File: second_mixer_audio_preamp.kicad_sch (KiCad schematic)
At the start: 34 parts, among them Q1301 MMBT3904, Q1302 MMBT3904, Q1303 MMBT3904, U1301 ADE-1

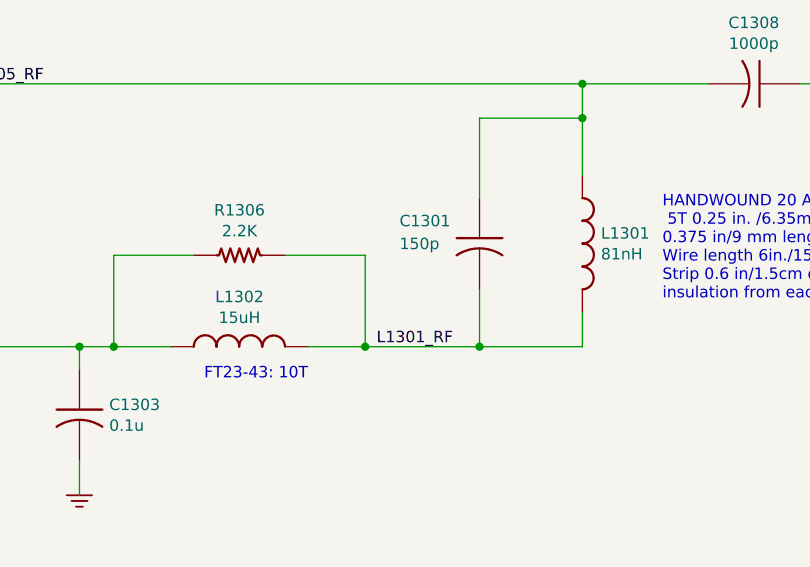
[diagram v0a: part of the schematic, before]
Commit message: Update pcb database to version 6
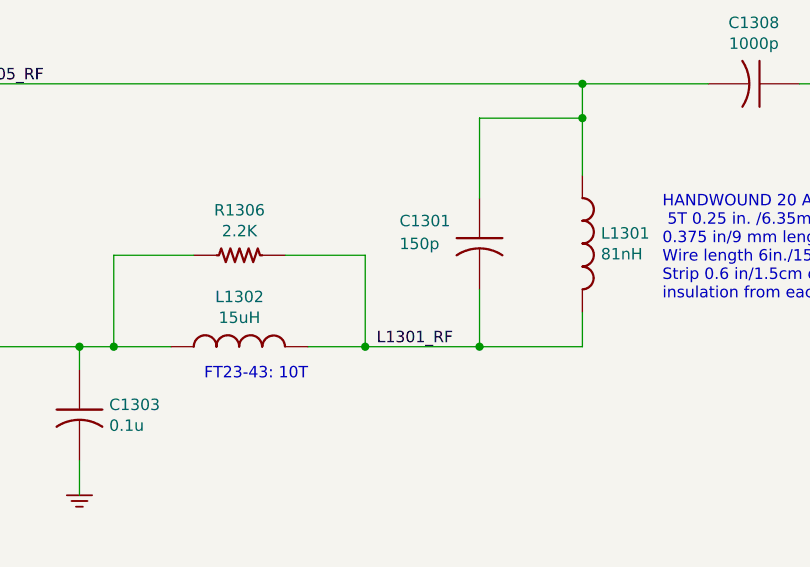
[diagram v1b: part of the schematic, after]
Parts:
- C1301: symbol Custom:C_US_0805_0.1UF_X7R_10%_50V_HS -> custom:C_US_0805_0.1UF_X7R_10%_50V_HS; PartNumber 800239-151 -> 800238-104
- C1302, C1304, C1305, C1306, C1307: symbol Custom:CP_US -> custom:CP_US; PartNumber 800267-226 -> 80000X-XXX
- C1303: symbol Custom:C_US_0805_0.1UF_X7R_10%_50V_HS -> custom:C_US_0805_0.1UF_X7R_10%_50V_HS
- C1308: symbol Custom:C_US -> custom:C_US; PartNumber 800239-102 -> 800063-XXX
- L1301: symbol Custom:L_US -> custom:L_US; PartNumber 800YYY-YYY -> 8000XX-XXX
- L1302: symbol Custom:L_US -> custom:L_US; PartNumber 800257-023 -> 8000XX-XXX
- Q1301, Q1302, Q1303: symbol Custom:MMBT3904 -> custom:MMBT3904
- R1301, R1304: symbol Custom:R_US_0805_1%_HS -> custom:R_US_0805_1%_HS; PartNumber 800235-180 -> 800235-XXX
- R1302, R1303, R1307, R1308: symbol Custom:R_US_0805_1%_HS -> custom:R_US_0805_1%_HS; PartNumber 800235-301 -> 800235-XXX
- R1305: symbol Custom:R_US_0805_1%_HS -> custom:R_US_0805_1%_HS; PartNumber 800235-360 -> 800235-XXX
- R1306: symbol Custom:R_US_0805_1%_HS -> custom:R_US_0805_1%_HS; PartNumber 800235-222 -> 800235-XXX
- R1309, R1310: symbol Custom:R_US_0805_1%_HS -> custom:R_US_0805_1%_HS; PartNumber 800235-151 -> 800235-XXX
- R1311: symbol Custom:R_US_0805_1%_HS -> custom:R_US_0805_1%_HS; PartNumber 800235-473 -> 800235-XXX
- R1312, R1314: symbol Custom:R_US_0805_1%_HS -> custom:R_US_0805_1%_HS; PartNumber 800235-102 -> 800235-XXX
- R1313, R1317: symbol Custom:R_US_0805_1%_HS -> custom:R_US_0805_1%_HS; PartNumber 800235-332 -> 800235-XXX
- R1315: symbol Custom:R_US_0805_1%_HS -> custom:R_US_0805_1%_HS; PartNumber 800235-103 -> 800235-XXX
- R1316: symbol Custom:R_US_0805_1%_HS -> custom:R_US_0805_1%_HS; PartNumber 800235-682 -> 800235-XXX
- R1318: symbol Custom:R_US_0805_1%_HS -> custom:R_US_0805_1%_HS; PartNumber 800235-101 -> 800235-XXX
- R1319: symbol Custom:R_US_0805_1%_HS -> custom:R_US_0805_1%_HS; PartNumber 800235-472 -> 800235-XXX
- TP1301: symbol Custom:TESTPINTPSQ025 -> custom:TESTPINTPSQ025
- U1301: symbol Custom:ADE-1 -> custom:ADE-1

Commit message: Fix BOM part number errors and out of sync footprints which happened during conversion from Kicad 5 to 6
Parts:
- C1301: PartNumber 800238-104 -> 800239-151
- C1302, C1304, C1305, C1306, C1307: PartNumber 80000X-XXX -> 800267-226
- C1308: PartNumber 800063-XXX -> 800239-103
- R1301, R1304: PartNumber 800235-XXX -> 800235-180
- R1302, R1303, R1307, R1308: PartNumber 800235-XXX -> 800235-301
- R1305: PartNumber 800235-XXX -> 800235-360
- R1306: PartNumber 800235-XXX -> 800235-222
- R1309, R1310: PartNumber 800235-XXX -> 800235-151
- R1311: PartNumber 800235-XXX -> 800235-473
- R1312, R1314: PartNumber 800235-XXX -> 800235-102
- R1313, R1317: PartNumber 800235-XXX -> 800235-332
- R1315: PartNumber 800235-XXX -> 800235-103
- R1316: PartNumber 800235-XXX -> 800235-682
- R1318: PartNumber 800235-XXX -> 800235-101
- R1319: PartNumber 800235-XXX -> 800235-472
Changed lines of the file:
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@@
       (effects (font (size 1.524 1.524)))
     )
-    (property "PartNumber" "800235-XXX" (id 4) (at 42.672 27.94 90)
+    (property "PartNumber" "800235-301" (id 4) (at 42.672 27.94 90)
       (effects (font (size 1.524 1.524)) hide)
     )
@@
       (effects (font (size 1.524 1.524)))
     )
-    (property "PartNumber" "800235-XXX" (id 4) (at 59.182 27.94 90)
+    (property "PartNumber" "800235-301" (id 4) (at 59.182 27.94 90)
       (effects (font (size 1.524 1.524)) hide)
     )
@@
       (effects (font (size 1.524 1.524)))
     )
-    (property "PartNumber" "800235-XXX" (id 4) (at 49.53 26.162 90)
+    (property "PartNumber" "800235-180" (id 4) (at 49.53 26.162 90)
       (effects (font (size 1.524 1.524)) hide)
     )
@@
       (effects (font (size 1.524 1.524)))
     )
-    (property "PartNumber" "800235-XXX" (id 4) (at 42.672 57.15 90)
+    (property "PartNumber" "800235-301" (id 4) (at 42.672 57.15 90)
       (effects (font (size 1.524 1.524)) hide)
     )
@@
       (effects (font (size 1.524 1.524)))
     )
-    (property "PartNumber" "800235-XXX" (id 4) (at 59.182 57.15 90)
+    (property "PartNumber" "800235-301" (id 4) (at 59.182 57.15 90)
       (effects (font (size 1.524 1.524)) hide)
     )
@@
       (effects (font (size 1.524 1.524)))
     )
-    (property "PartNumber" "800235-XXX" (id 4) (at 49.53 55.372 90)
+    (property "PartNumber" "800235-180" (id 4) (at 49.53 55.372 90)
       (effects (font (size 1.524 1.524)) hide)
     )
@@
       (effects (font (size 1.524 1.524)))
     )
-    (property "PartNumber" "800235-XXX" (id 4) (at 111.252 57.15 90)
+    (property "PartNumber" "800235-151" (id 4) (at 111.252 57.15 90)
       (effects (font (size 1.524 1.524)) hide)
     )
@@
       (effects (font (size 1.524 1.524)))
     )
-    (property "PartNumber" "800235-XXX" (id 4) (at 127.762 57.15 90)
+    (property "PartNumber" "800235-151" (id 4) (at 127.762 57.15 90)
       (effects (font (size 1.524 1.524)) hide)
     )
@@
       (effects (font (size 1.524 1.524)))
     )
-    (property "PartNumber" "800235-XXX" (id 4) (at 118.11 55.372 90)
+    (property "PartNumber" "800235-360" (id 4) (at 118.11 55.372 90)
       (effects (font (size 1.524 1.524)) hide)
     )
@@
       (effects (font (size 1.524 1.524)))
     )
-    (property "PartNumber" "80000X-XXX" (id 4) (at 59.69 76.2 0)
+    (property "PartNumber" "800267-226" (id 4) (at 59.69 76.2 0)
       (effects (font (size 1.524 1.524)) hide)
     )
@@
       (effects (font (size 1.524 1.524)))
     )
-    (property "PartNumber" "800235-XXX" (id 4) (at 41.402 133.35 90)
+    (property "PartNumber" "800235-332" (id 4) (at 41.402 133.35 90)
       (effects (font (size 1.524 1.524)) hide)
     )
@@
       (effects (font (size 1.524 1.524)))
     )
-    (property "PartNumber" "800235-XXX" (id 4) (at 73.152 100.33 90)
+    (property "PartNumber" "800235-332" (id 4) (at 73.152 100.33 90)
       (effects (font (size 1.524 1.524)) hide)
     )
@@
       (effects (font (size 1.524 1.524)))
     )
-    (property "PartNumber" "80000X-XXX" (id 4) (at 54.61 107.95 0)
+    (property "PartNumber" "800267-226" (id 4) (at 54.61 107.95 0)
       (effects (font (size 1.524 1.524)) hide)
     )
@@
       (effects (font (size 1.524 1.524)))
     )
-    (property "PartNumber" "800235-XXX" (id 4) (at 80.01 118.872 90)
+    (property "PartNumber" "800235-103" (id 4) (at 80.01 118.872 90)
       (effects (font (size 1.524 1.524)) hide)
     )
@@
       (effects (font (size 1.524 1.524)))
     )
-    (property "PartNumber" "800235-XXX" (id 4) (at 94.742 118.11 90)
+    (property "PartNumber" "800235-682" (id 4) (at 94.742 118.11 90)
       (effects (font (size 1.524 1.524)) hide)
     )
@@
       (effects (font (size 1.524 1.524)))
     )
-    (property "PartNumber" "800235-XXX" (id 4) (at 111.252 92.71 90)
+    (property "PartNumber" "800235-473" (id 4) (at 111.252 92.71 90)
       (effects (font (size 1.524 1.524)) hide)
     )
@@
       (effects (font (size 1.524 1.524)))
     )
-    (property "PartNumber" "80000X-XXX" (id 4) (at 110.49 105.41 0)
+    (property "PartNumber" "800267-226" (id 4) (at 110.49 105.41 0)
       (effects (font (size 1.524 1.524)) hide)
     )
@@
       (effects (font (size 1.524 1.524)))
     )
-    (property "PartNumber" "800235-XXX" (id 4) (at 135.382 140.97 90)
+    (property "PartNumber" "800235-472" (id 4) (at 135.382 140.97 90)
       (effects (font (size 1.524 1.524)) hide)
     )
@@
       (effects (font (size 1.524 1.524)))
     )
-    (property "PartNumber" "800235-XXX" (id 4) (at 122.682 140.97 90)
+    (property "PartNumber" "800235-101" (id 4) (at 122.682 140.97 90)
       (effects (font (size 1.524 1.524)) hide)
     )
@@
       (effects (font (size 1.524 1.524)))
     )
-    (property "PartNumber" "80000X-XXX" (id 4) (at 121.92 148.59 0)
+    (property "PartNumber" "800267-226" (id 4) (at 121.92 148.59 0)
       (effects (font (size 1.524 1.524)) hide)
     )
@@
       (effects (font (size 1.524 1.524)))
     )
-    (property "PartNumber" "800235-XXX" (id 4) (at 135.382 92.71 90)
+    (property "PartNumber" "800235-102" (id 4) (at 135.382 92.71 90)
       (effects (font (size 1.524 1.524)) hide)
     )
@@
       (effects (font (size 1.524 1.524)))
     )
-    (property "PartNumber" "800235-XXX" (id 4) (at 135.382 110.49 90)
+    (property "PartNumber" "800235-102" (id 4) (at 135.382 110.49 90)
       (effects (font (size 1.524 1.524)) hide)
     )
@@
       (effects (font (size 1.524 1.524)))
     )
-    (property "PartNumber" "80000X-XXX" (id 4) (at 123.19 105.41 0)
+    (property "PartNumber" "800267-226" (id 4) (at 123.19 105.41 0)
       (effects (font (size 1.524 1.524)) hide)
     )
@@
       (effects (font (size 1.524 1.524)))
     )
-    (property "PartNumber" "800238-104" (id 4) (at 194.31 54.61 0)
+    (property "PartNumber" "800239-151" (id 4) (at 194.31 54.61 0)
       (effects (font (size 1.524 1.524)) hide)
     )
@@
       (effects (font (size 1.524 1.524)))
     )
-    (property "PartNumber" "800063-XXX" (id 4) (at 238.76 50.8 0)
+    (property "PartNumber" "800239-103" (id 4) (at 238.76 50.8 0)
       (effects (font (size 1.524 1.524)) hide)
     )
@@
       (effects (font (size 1.524 1.524)))
     )
-    (property "PartNumber" "800235-XXX" (id 4) (at 170.18 74.422 90)
-      (effects (font (size 1.524 1.524)) hide)
-    )
+    (property "PartNumber" "800235-222" (id 4) (at 170.18 74.422 90)
+      (effects (font (size 1.524 1.524)) hide)
+    )

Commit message: trx_mobo_concept_2_B. Change design to use a dedicated 8V supply for the 2SC3357 parts. Add S-Meter connector. Change mic connector to 3 pins and add 8V sopower supply to pin 3.
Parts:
- removed TP1301: TESTPINTPSQ025, mods:TESTPIN, symbol custom:TESTPINTPSQ025
- C2001: renamed from C1308; value 1000p -> (none); footprint Capacitor_SMD:C_0805_2012Metric_Pad1.15x1.40mm_HandSolder -> (none); PartNumber 800239-103 -> 800239-102
- C2002: renamed from C1301; value 150p -> (none); footprint Capacitor_SMD:C_0805_2012Metric_Pad1.15x1.40mm_HandSolder -> (none)
- C2003: renamed from C1302; value 22u -> (none); footprint Capacitor_SMD:CP_Elec_6.3x5.7 -> (none)
- C2004: renamed from C1303; value 0.1u -> (none); footprint Capacitor_SMD:C_0805_2012Metric_Pad1.15x1.40mm_HandSolder -> (none)
- C2005: renamed from C1304; value 22u -> (none); footprint Capacitor_SMD:CP_Elec_6.3x5.7 -> (none)
- C2006: renamed from C1305; value 22u -> (none); footprint Capacitor_SMD:CP_Elec_6.3x5.7 -> (none)
- C2007: renamed from C1306; value 22u -> (none); footprint Capacitor_SMD:CP_Elec_6.3x5.7 -> (none)
- C2008: renamed from C1307; value 22u -> (none); footprint Capacitor_SMD:CP_Elec_6.3x5.7 -> (none)
- L2001: renamed from L1301; value 81nH -> (none); footprint mods:AIR_CORE_9MMX6.3MM -> (none); PartNumber 8000XX-XXX -> 8XXXXX-XXX
- L2002: renamed from L1302; value 15uH -> (none); footprint mods:TOROID_T37_VERT -> (none); PartNumber 8000XX-XXX -> 800257-023
- Q2001: renamed from Q1301; value MMBT3904 -> (none); footprint mods:SOT23-3-SAR -> (none)
- Q2002: renamed from Q1302; value MMBT3904 -> (none); footprint mods:SOT23-3-SAR -> (none)
- Q2003: renamed from Q1303; value MMBT3904 -> (none); footprint mods:SOT23-3-SAR -> (none)
- R2001: renamed from R1301; value 18 -> (none); footprint Resistor_SMD:R_0805_2012Metric_Pad1.15x1.40mm_HandSolder -> (none)
- R2002: renamed from R1302; value 300 -> (none); footprint Resistor_SMD:R_0805_2012Metric_Pad1.15x1.40mm_HandSolder -> (none)
- R2003: renamed from R1303; value 300 -> (none); footprint Resistor_SMD:R_0805_2012Metric_Pad1.15x1.40mm_HandSolder -> (none)
- R2004: renamed from R1304; value 18 -> (none); footprint Resistor_SMD:R_0805_2012Metric_Pad1.15x1.40mm_HandSolder -> (none)
- R2005: renamed from R1305; value 36 -> (none); footprint Resistor_SMD:R_0805_2012Metric_Pad1.15x1.40mm_HandSolder -> (none)
- R2006: renamed from R1307; value 300 -> (none); footprint Resistor_SMD:R_0805_2012Metric_Pad1.15x1.40mm_HandSolder -> (none)
- R2007: renamed from R1308; value 300 -> (none); footprint Resistor_SMD:R_0805_2012Metric_Pad1.15x1.40mm_HandSolder -> (none)
- R2008: renamed from R1309; value 150 -> (none); footprint Resistor_SMD:R_0805_2012Metric_Pad1.15x1.40mm_HandSolder -> (none)
- R2009: renamed from R1310; value 150 -> (none); footprint Resistor_SMD:R_0805_2012Metric_Pad1.15x1.40mm_HandSolder -> (none)
- R2010: renamed from R1306; value 2.2K -> (none); footprint Resistor_SMD:R_0805_2012Metric_Pad1.15x1.40mm_HandSolder -> (none)
- R2011: renamed from R1311; value 47K -> (none); footprint Resistor_SMD:R_0805_2012Metric_Pad1.15x1.40mm_HandSolder -> (none)
- R2012: renamed from R1312; value 1K -> (none); footprint Resistor_SMD:R_0805_2012Metric_Pad1.15x1.40mm_HandSolder -> (none)
- R2013: renamed from R1313; value 3.3K -> (none); footprint Resistor_SMD:R_0805_2012Metric_Pad1.15x1.40mm_HandSolder -> (none)
- R2014: renamed from R1314; value 1K -> (none); footprint Resistor_SMD:R_0805_2012Metric_Pad1.15x1.40mm_HandSolder -> (none)
- R2015: renamed from R1315; value 10K -> (none); footprint Resistor_SMD:R_0805_2012Metric_Pad1.15x1.40mm_HandSolder -> (none)
- R2016: renamed from R1316; value 6.8K -> (none); footprint Resistor_SMD:R_0805_2012Metric_Pad1.15x1.40mm_HandSolder -> (none)
- R2017: renamed from R1317; value 3.3K -> (none); footprint Resistor_SMD:R_0805_2012Metric_Pad1.15x1.40mm_HandSolder -> (none)
- R2018: renamed from R1318; value 100 -> (none); footprint Resistor_SMD:R_0805_2012Metric_Pad1.15x1.40mm_HandSolder -> (none)
- R2019: renamed from R1319; value 4.7K -> (none); footprint Resistor_SMD:R_0805_2012Metric_Pad1.15x1.40mm_HandSolder -> (none)
- U2001: renamed from U1301; value ADE-1 -> (none); footprint mods:MCL-6-SMD_7R97X5R59 -> (none)
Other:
- note added: "#30 AWG"
- note added: "HANDWOUND 20 AWG/ 0.8mm bus wire 5T 0.25 in. /6.35mm drill bit 0.375 in/9 mm length Wire length 6in./15cm."
- note removed: "HANDWOUND 20 AWG/ 0.8mm enamel 5T 0.25 in. /6.35mm drill bit 0.375 in/9 mm length Wire length 6in./15cm. Strip 0.6 in/1.5cm of insulation from each end"
